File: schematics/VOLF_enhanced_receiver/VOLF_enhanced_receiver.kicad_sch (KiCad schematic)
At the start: 13 parts, among them J1 AudioJack3, J2 MCU DP2, J3 MCU A0, J4 MCU GND, J5 MCU DP3, K1 Relay NC, SW1 SW_Push

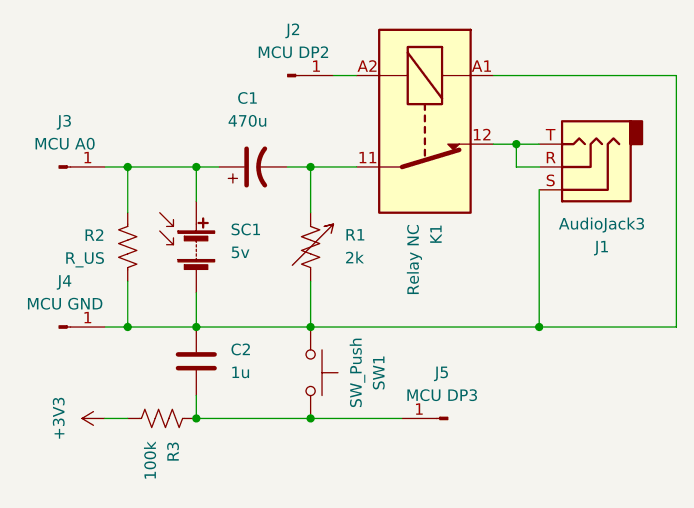
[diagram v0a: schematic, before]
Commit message: updated schematics
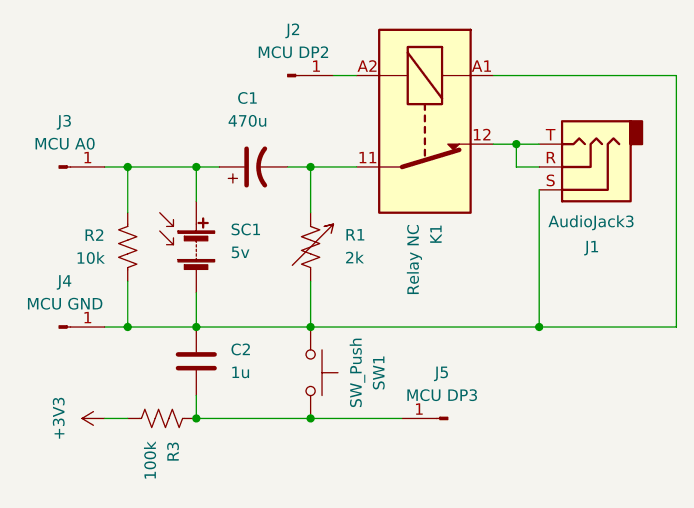
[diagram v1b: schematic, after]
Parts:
- R2: value R_US -> 10k
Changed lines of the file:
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@@
 		(on_board yes)
 		(dnp no)
-		(fields_autoplaced yes)
 		(property "Reference" "J1"
-			(at 133.985 67.31 0)
-			(effects
-				(font
-					(size 1.27 1.27)
-				)
+			(at 132.08 67.31 0)
+			(effects
+				(font
+					(size 1.27 1.27)
+				)
+				(justify right)
 			)
 		)
 		(property "Value" "AudioJack3"
-			(at 133.985 64.77 0)
-			(effects
-				(font
-					(size 1.27 1.27)
-				)
+			(at 128.016 64.516 0)
+			(effects
+				(font
+					(size 1.27 1.27)
+				)
+				(justify right)
 			)
 		)
@@
 				)
 			)
+			(project "VOLF_enhanced_receiver"
+				(path "/d5ab7ffb-ff24-4b3e-a886-a1c4ffbedf87"
+					(reference "J1")
+					(unit 1)
+				)
+			)
 		)
 	)
@@
 			(project ""
 				(path "/b58e6bc4-c379-4e3c-959a-c8afc3fb126f"
+					(reference "SC1")
+					(unit 1)
+				)
+			)
+			(project "VOLF_enhanced_receiver"
+				(path "/d5ab7ffb-ff24-4b3e-a886-a1c4ffbedf87"
 					(reference "SC1")
 					(unit 1)
@@
 				)
 			)
+			(project "VOLF_enhanced_receiver"
+				(path "/d5ab7ffb-ff24-4b3e-a886-a1c4ffbedf87"
+					(reference "R?")
+					(unit 1)
+				)
+			)
 		)
 	)
@@
 			)
 		)
-		(property "Value" "R_US"
+		(property "Value" "10k"
 			(at 78.74 68.5799 0)
 			(effects
@@
 					(reference "C1")
 					(unit 1)
+				)
+			)
+			(project "VOLF_enhanced_receiver"
+				(path "/d5ab7ffb-ff24-4b3e-a886-a1c4ffbedf87"
+					(reference "C1")
+					(unit 1)
